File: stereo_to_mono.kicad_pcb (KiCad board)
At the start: 2 copper layers, 58 x 24 mm, 8 parts, among them J1 AudioJack3, J2 AudioJack3, J3 Conn_01x03, J4 Conn_01x03

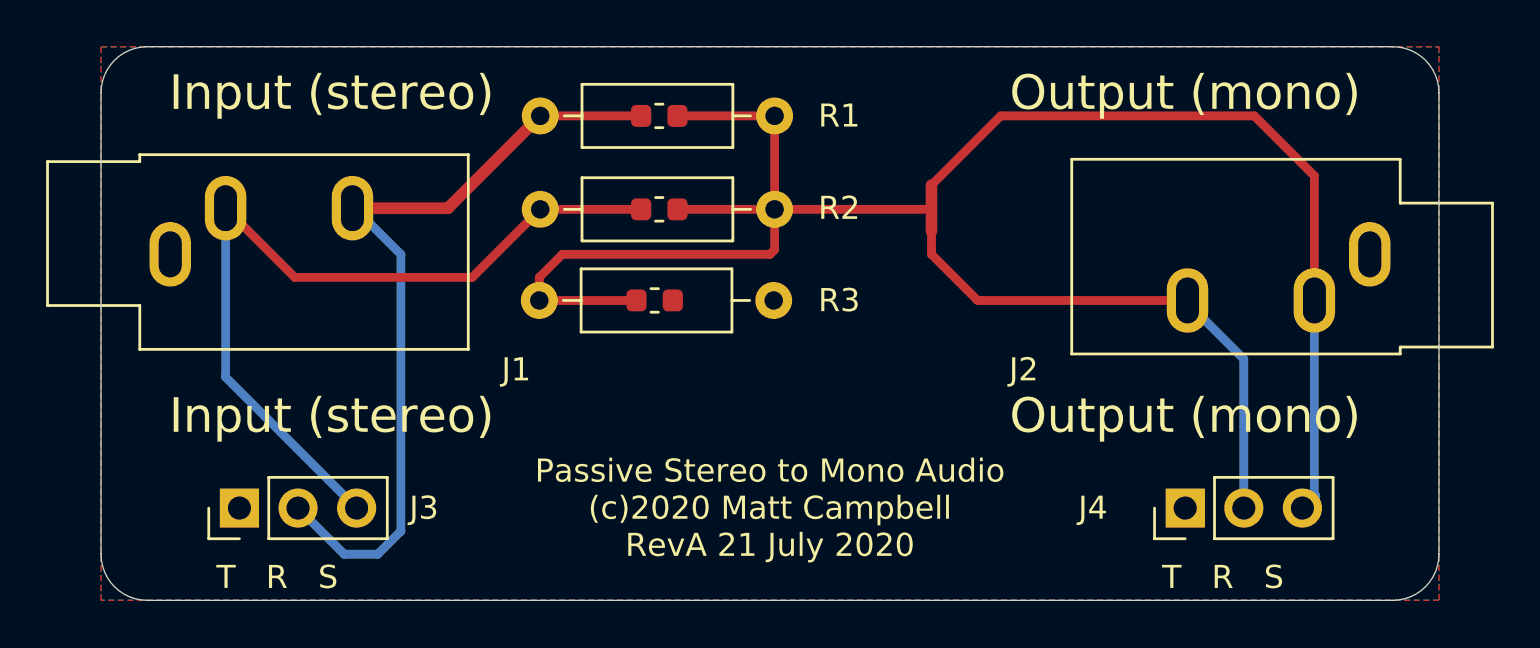
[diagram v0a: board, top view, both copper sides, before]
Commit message: Fix connects on teat headers
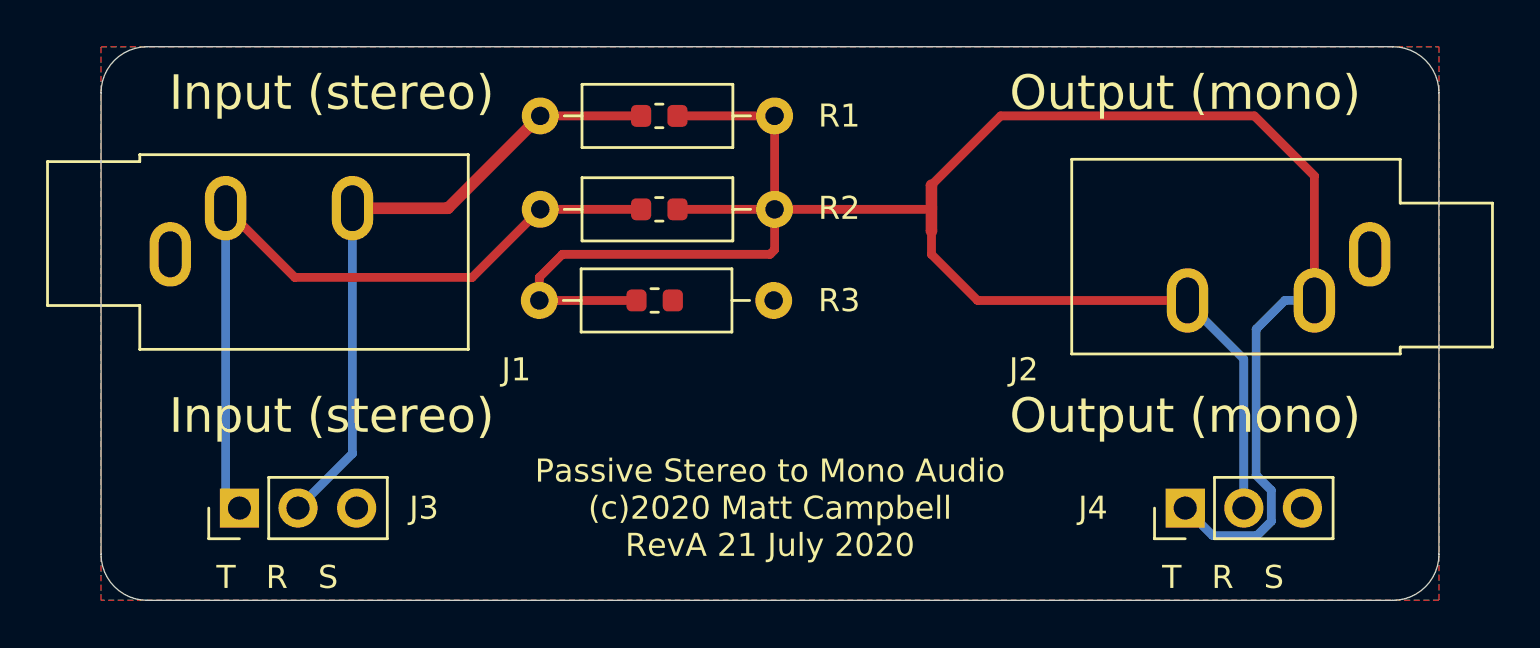
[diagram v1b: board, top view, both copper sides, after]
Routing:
- net Net-(J2-PadT): track 33.5 -> 40.4 mm
- net Net-(J1-PadR): track 34.8 -> 28.2 mm
- net Net-(J1-PadT): track 35.8 -> 33.7 mm
